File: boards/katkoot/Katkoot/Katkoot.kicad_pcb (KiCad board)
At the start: 2 copper layers, 48.9 x 51.2 mm, 16 parts, among them J1 Conn_01x12_Female, J2 Conn_01x12_Female, J3 Conn_01x06_Female, U1 TCR2EF19,LM(CT, U2 PMW3360DM-T2QU

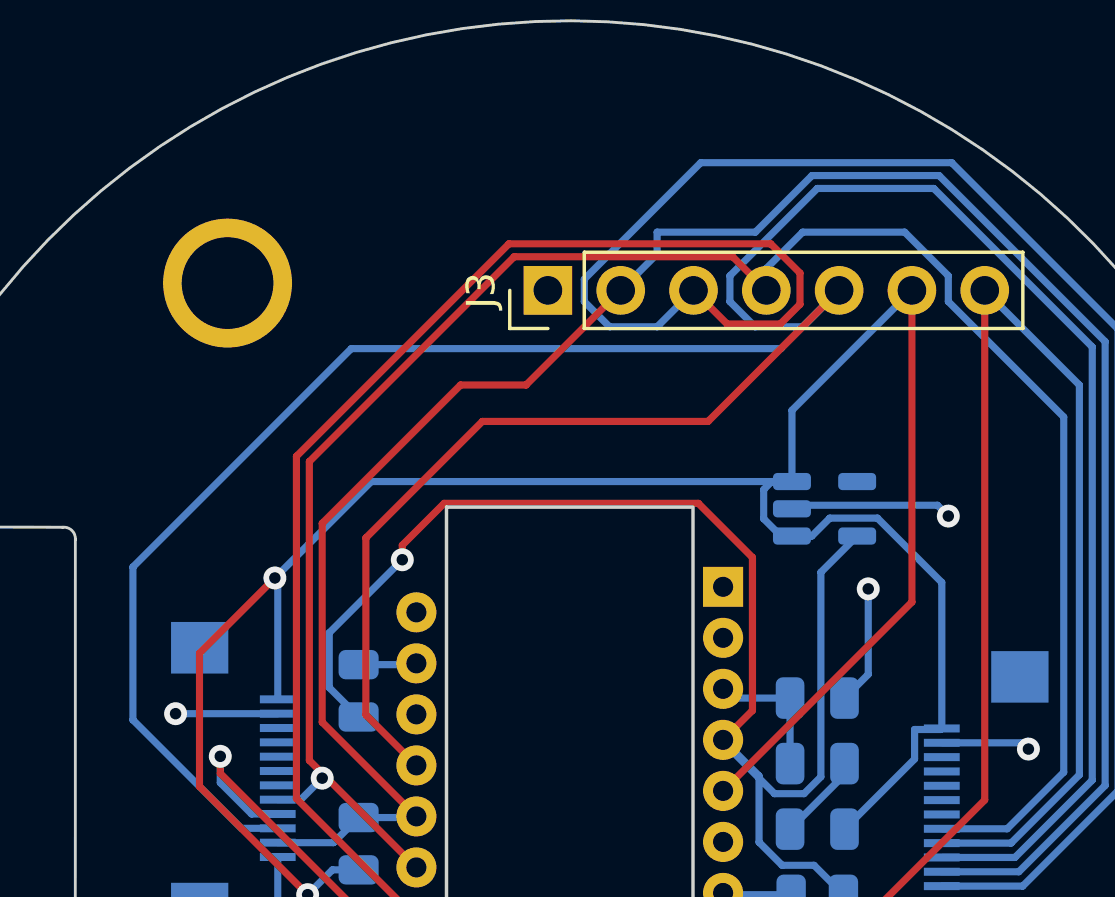
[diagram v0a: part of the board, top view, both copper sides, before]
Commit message: fixed gnd issue in katkoot
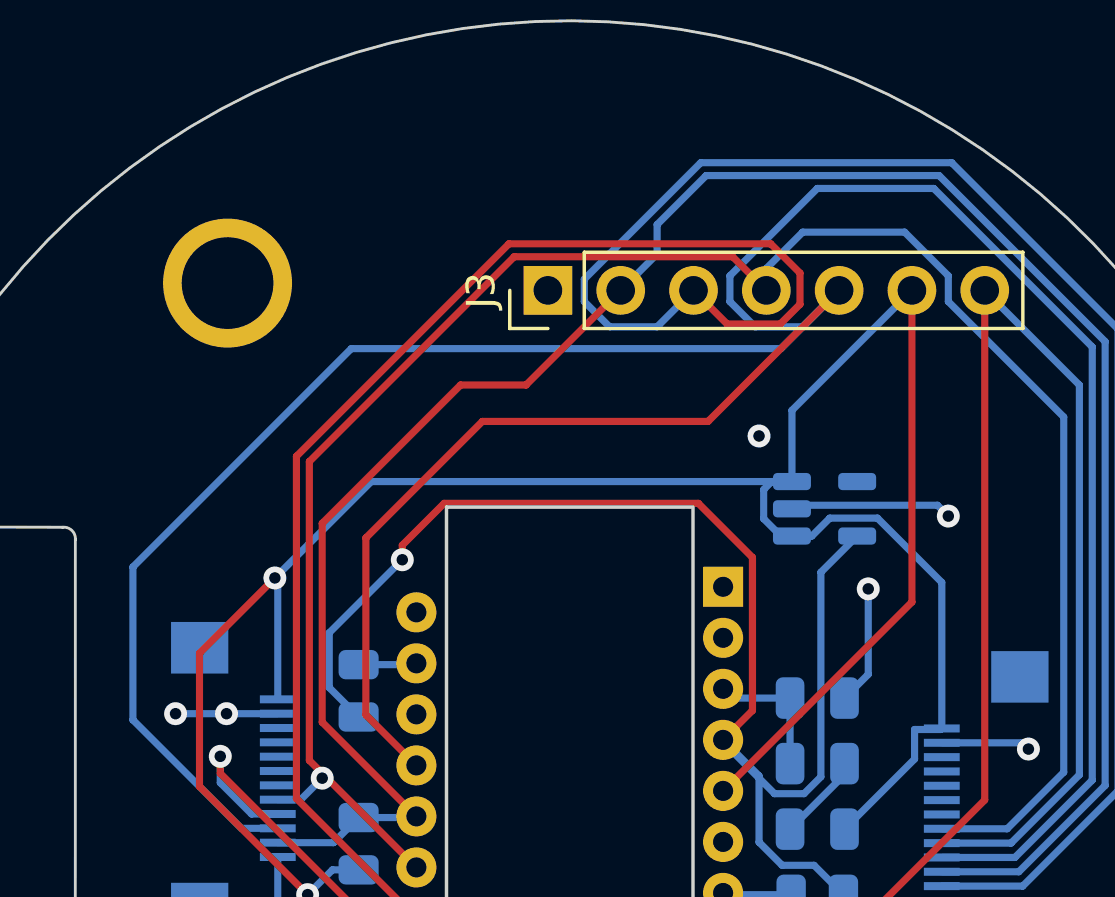
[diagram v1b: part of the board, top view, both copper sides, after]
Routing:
- net GND: vias 4 -> 6
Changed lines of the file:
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@@
     (attr board_only exclude_from_pos_files exclude_from_bom)
     (fp_text reference "kibuzzard-63793EB1" (at 0 3.891492 90) (layer "B.SilkS") hide
-      (effects (font (size 0 0)) (justify mirror))
+      (effects (font (size 0 0) (thickness 0.15)) (justify mirror))
     )
     (fp_text value "G***" (at 0 -3.891492 90) (layer "B.SilkS") hide
-      (effects (font (size 0 0)) (justify mirror))
+      (effects (font (size 0 0) (thickness 0.15)) (justify mirror))
     )
     (fp_poly (pts
@@
     (attr board_only exclude_from_pos_files exclude_from_bom)
     (fp_text reference "kibuzzard-63793EC8" (at 0 3.891492 90) (layer "B.SilkS") hide
-      (effects (font (size 0 0)) (justify mirror))
+      (effects (font (size 0 0) (thickness 0.15)) (justify mirror))
     )
     (fp_text value "G***" (at 0 -3.891492 90) (layer "B.SilkS") hide
-      (effects (font (size 0 0)) (justify mirror))
+      (effects (font (size 0 0) (thickness 0.15)) (justify mirror))
     )
     (fp_poly (pts
@@
   (via (at 167.64 54.864) (size 0.8) (drill 0.4) (layers "F.Cu" "B.Cu") (net 2))
   (via (at 140.68 61.758) (size 0.8) (drill 0.4) (layers "F.Cu" "B.Cu") (net 2))
+  (via (at 142.458 61.758) (size 0.8) (drill 0.4) (layers "F.Cu" "B.Cu") (net 2))
+  (via (at 161.036 52.07) (size 0.8) (drill 0.4) (layers "F.Cu" "B.Cu") (free) (net 2))
   (via (at 170.434 62.992) (size 0.8) (drill 0.4) (layers "F.Cu" "B.Cu") (net 2))
   (segment (start 162.30854 54.48596) (end 167.26196 54.48596) (width 0.25) (layer "B.Cu") (net 2))
   (segment (start 164.018 63.886) (end 162.118 65.786) (width 0.25) (layer "B.Cu") (net 2))
   (segment (start 164.018 61.214) (end 164.846 60.386) (width 0.25) (layer "B.Cu") (net 2))
-  (segment (start 144.246 61.758) (end 140.68 61.758) (width 0.25) (layer "B.Cu") (net 2))
+  (segment (start 144.246 61.758) (end 142.458 61.758) (width 0.25) (layer "B.Cu") (net 2))
   (segment (start 170.216 62.774) (end 167.412 62.774) (width 0.25) (layer "B.Cu") (net 2))
   (segment (start 170.434 62.992) (end 170.216 62.774) (width 0.25) (layer "B.Cu") (net 2))
   (segment (start 162.1845 54.61) (end 162.30854 54.48596) (width 0.25) (layer "B.Cu") (net 2))
+  (segment (start 142.458 61.758) (end 140.68 61.758) (width 0.25) (layer "B.Cu") (net 2))
   (segment (start 164.846 60.386) (end 164.846 57.404) (width 0.25) (layer "B.Cu") (net 2))
   (segment (start 164.018 63.5) (end 164.018 63.886) (width 0.25) (layer "B.Cu") (net 2))
@@
   (segment (start 145.796 55.118) (end 150.622 50.292) (width 0.25) (layer "F.Cu") (net 13))
   (segment (start 152.908 50.292) (end 156.21 46.99) (width 0.25) (layer "F.Cu") (net 13))
-  (segment (start 162.881802 42.98448) (end 160.908282 44.958) (width 0.25) (layer "B.Cu") (net 13))
+  (segment (start 167.412 67.274) (end 170.099765 67.274) (width 0.25) (layer "B.Cu") (net 13))
+  (segment (start 173.11104 48.777323) (end 167.318197 42.98448) (width 0.25) (layer "B.Cu") (net 13))
+  (segment (start 170.099765 67.274) (end 173.11104 64.262725) (width 0.25) (layer "B.Cu") (net 13))
+  (segment (start 157.48 44.694708) (end 157.48 45.72) (width 0.25) (layer "B.Cu") (net 13))
   (segment (start 147.066 65.3815) (end 149.0425 65.3815) (width 0.25) (layer "B.Cu") (net 13))
-  (segment (start 170.099765 67.274) (end 173.11104 64.262725) (width 0.25) (layer "B.Cu") (net 13))
+  (segment (start 159.190228 42.98448) (end 157.48 44.694708) (width 0.25) (layer "B.Cu") (net 13))
   (segment (start 173.11104 64.262725) (end 173.11104 48.777323) (width 0.25) (layer "B.Cu") (net 13))
-  (segment (start 157.48 44.958) (end 157.48 45.72) (width 0.25) (layer "B.Cu") (net 13))
-  (segment (start 167.412 67.274) (end 170.099765 67.274) (width 0.25) (layer "B.Cu") (net 13))
   (segment (start 157.48 45.72) (end 156.21 46.99) (width 0.25) (layer "B.Cu") (net 13))
-  (segment (start 167.318197 42.98448) (end 162.881802 42.98448) (width 0.25) (layer "B.Cu") (net 13))
   (segment (start 144.246 66.258) (end 146.1895 66.258) (width 0.25) (layer "B.Cu") (net 13))
-  (segment (start 173.11104 48.777323) (end 167.318197 42.98448) (width 0.25) (layer "B.Cu") (net 13))
   (segment (start 146.1895 66.258) (end 147.066 65.3815) (width 0.25) (layer "B.Cu") (net 13))
+  (segment (start 167.318197 42.98448) (end 159.190228 42.98448) (width 0.25) (layer "B.Cu") (net 13))
   (segment (start 149.0425 65.3815) (end 149.082 65.342) (width 0.25) (layer "B.Cu") (net 13))
-  (segment (start 160.908282 44.958) (end 157.48 44.958) (width 0.25) (layer "B.Cu") (net 13))
   (segment (start 159.924511 48.164511) (end 161.776499 48.164511) (width 0.25) (layer "F.Cu") (net 14))
   (segment (start 162.464511 47.476499) (end 162.464511 46.386511) (width 0.25) (layer "F.Cu") (net 14))
